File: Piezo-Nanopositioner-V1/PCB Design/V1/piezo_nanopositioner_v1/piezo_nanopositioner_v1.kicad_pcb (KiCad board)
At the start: 4 copper layers, 187.2 x 72.2 mm, 101 parts, among them J101 Conn_01x03_Pin, J201 Conn_01x10_Pin, J202 RF2-04A-T-00-50-G, J301 Conn_01x10_Pin, J302 RF2-04A-T-00-50-G, J401 Conn_01x10_Pin, J402 RF2-04A-T-00-50-G, U201 TL431AIDBZR, U202 DAC0800LCM, U203 TDA2050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

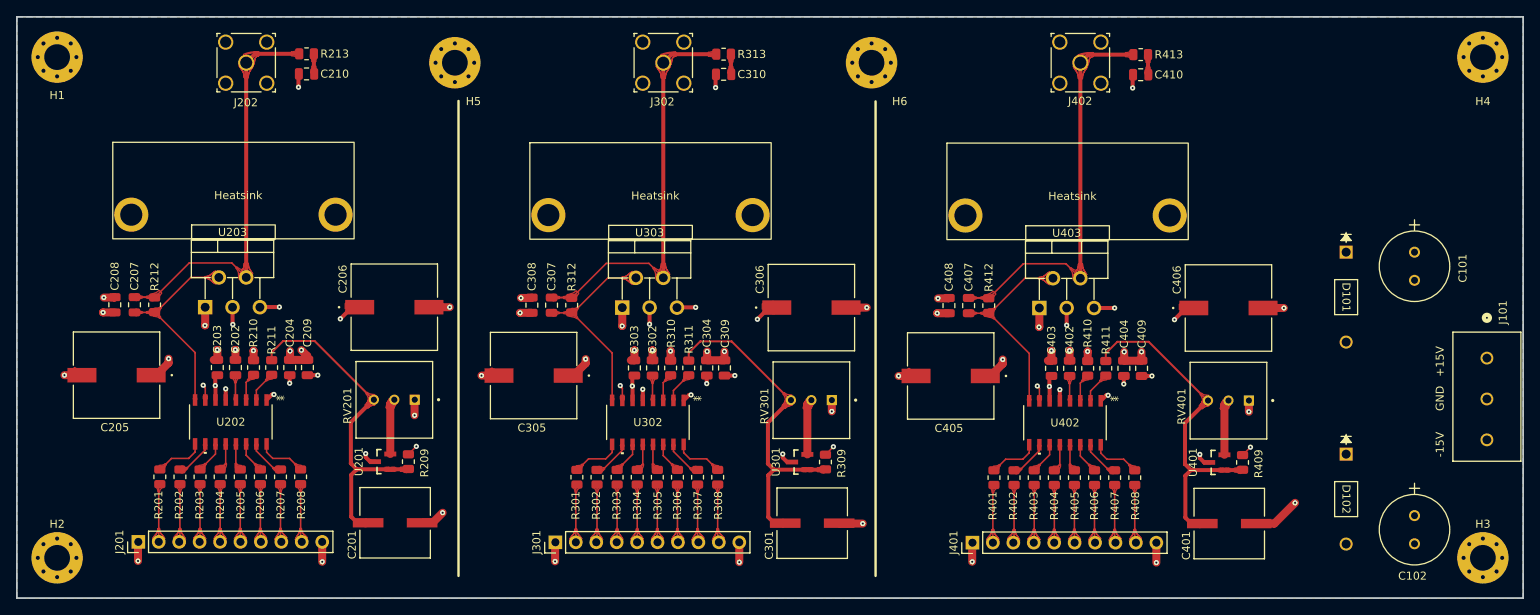
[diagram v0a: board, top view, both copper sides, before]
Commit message: added much needed polarity markings on silkscreen. Added testing rig files for testing your piezo element, clamps down the piezo and reads accelerometer data & temperatre (thermistor). Also added firmware for controlling piezo motion via Arduino Mega.
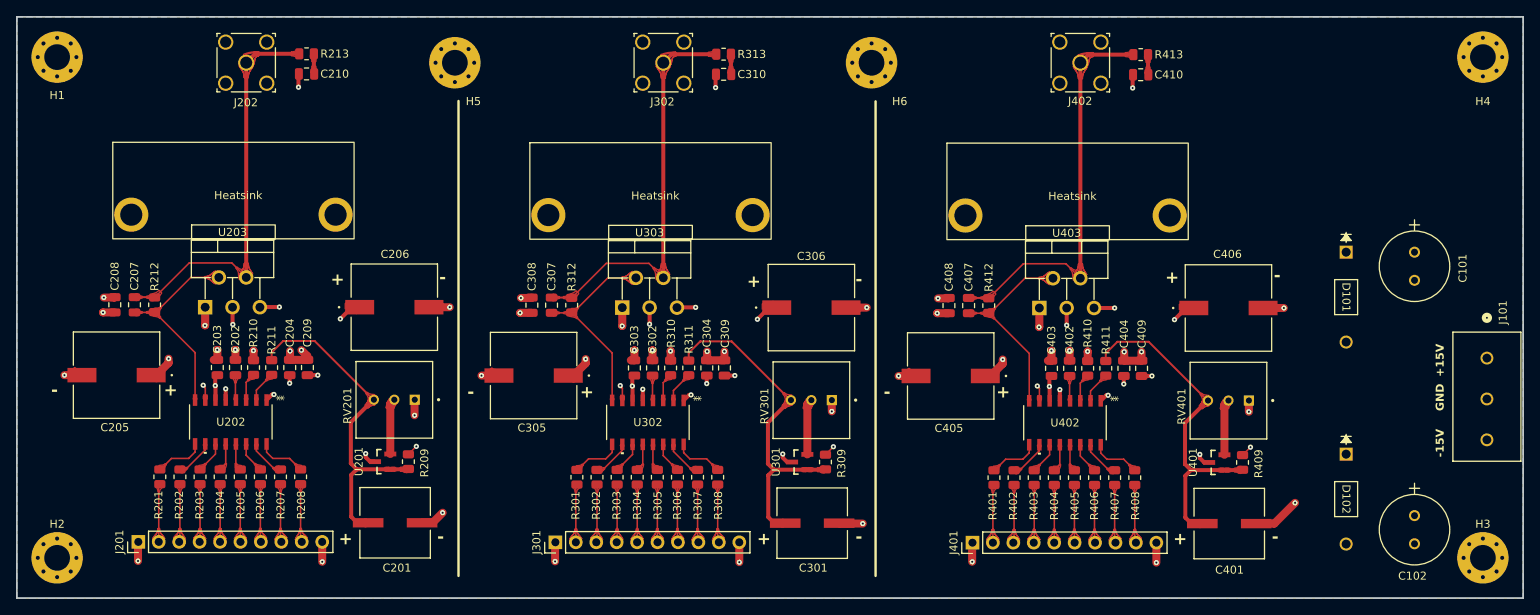
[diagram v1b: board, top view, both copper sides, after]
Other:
- board text added: "+"
- board text added: "-"
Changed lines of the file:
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@@
 		(tags "EEE-FC1E470P ")
 		(property "Reference" "C401"
-			(at -5.3528 2.75 90)
+			(at 0.03 5.76 0)
 			(unlocked yes)
 			(layer "F.SilkS")
@@
 		(tags "EEH-ZS1E471P ")
 		(property "Reference" "C306"
-			(at -6.4 -3.5 90)
+			(at -0.02 -6.39 0)
 			(unlocked yes)
 			(layer "F.SilkS")
@@
 		(tags "EEE-FC1E470P ")
 		(property "Reference" "C301"
-			(at -5.3528 2.75 90)
+			(at 0.13 5.56 0)
 			(unlocked yes)
 			(layer "F.SilkS")
@@
 		(tags "EEH-ZS1E471P ")
 		(property "Reference" "C206"
-			(at -6.4 -3.5 90)
+			(at 0.08 -6.59 0)
 			(unlocked yes)
 			(layer "F.SilkS")
@@
 		(tags "EEE-FC1E470P ")
 		(property "Reference" "C201"
-			(at -5.3528 2.75 90)
+			(at 0.23 5.61 0)
 			(unlocked yes)
 			(layer "F.SilkS")
@@
 		(tags "EEH-ZS1E471P ")
 		(property "Reference" "C406"
-			(at -6.4 -3.5 90)
+			(at -0.12 -6.69 0)
 			(unlocked yes)
 			(layer "F.SilkS")
@@
 		(layer "Edge.Cuts")
 	)
+	(gr_text "+"
+		(at 192 91 0)
+		(layer "F.SilkS")
+		(effects
+			(font
+				(size 1.5 1.5)
+				(thickness 0.375)
+				(bold yes)
+			)
+			(justify left bottom)
+		)
+	)
 	(gr_text "+15V"
 		(at 247.75 88.25 90)
@@
 			(font
 				(size 1 1)
-				(thickness 0.1)
+				(thickness 0.25)
+				(bold yes)
+			)
+			(justify left bottom)
+		)
+	)
+	(gr_text "-"
+		(at 226.5 76.5 0)
+		(layer "F.SilkS")
+		(effects
+			(font
+				(size 1.5 1.5)
+				(thickness 0.375)
+				(bold yes)
+			)
+			(justify left bottom)
+		)
+	)
+	(gr_text "-"
+		(at 174.5 77 0)
+		(layer "F.SilkS")
+		(effects
+			(font
+				(size 1.5 1.5)
+				(thickness 0.375)
+				(bold yes)
+			)
+			(justify left bottom)
+		)
+	)
+	(gr_text "-"
+		(at 74.5 90.75 0)
+		(layer "F.SilkS")
+		(effects
+			(font
+				(size 1.5 1.5)
+				(thickness 0.375)
+				(bold yes)
 			)
 			(justify left bottom)
@@
 			(font
 				(size 1 1)
-				(thickness 0.1)
+				(thickness 0.25)
+				(bold yes)
+			)
+			(justify left bottom)
+		)
+	)
+	(gr_text "+"
+		(at 140.25 91 0)
+		(layer "F.SilkS")
+		(effects
+			(font
+				(size 1.5 1.5)
+				(thickness 0.375)
+				(bold yes)
+			)
+			(justify left bottom)
+		)
+	)
+	(gr_text "+"
+		(at 214 109.25 0)
+		(layer "F.SilkS")
+		(effects
+			(font
+				(size 1.5 1.5)
+				(thickness 0.375)
+				(bold yes)
+			)
+			(justify left bottom)
+		)
+	)
+	(gr_text "-"
+		(at 122.5 109 0)
+		(layer "F.SilkS")
+		(effects
+			(font
+				(size 1.5 1.5)
+				(thickness 0.375)
+				(bold yes)
+			)
+			(justify left bottom)
+		)
+	)
+	(gr_text "+"
+		(at 161 77.25 0)
+		(layer "F.SilkS")
+		(effects
+			(font
+				(size 1.5 1.5)
+				(thickness 0.375)
+				(bold yes)
+			)
+			(justify left bottom)
+		)
+	)
+	(gr_text "+"
+		(at 88.5 90.75 0)
+		(layer "F.SilkS")
+		(effects
+			(font
+				(size 1.5 1.5)
+				(thickness 0.375)
+				(bold yes)
+			)
+			(justify left bottom)
+		)
+	)
+	(gr_text "+"
+		(at 109.25 77 0)
+		(layer "F.SilkS")
+		(effects
+			(font
+				(size 1.5 1.5)
+				(thickness 0.375)
+				(bold yes)
+			)
+			(justify left bottom)
+		)
+	)
+	(gr_text "-"
+		(at 178 91 0)
+		(layer "F.SilkS")
+		(effects
+			(font
+				(size 1.5 1.5)
+				(thickness 0.375)
+				(bold yes)
+			)
+			(justify left bottom)
+		)
+	)
+	(gr_text "+"
+		(at 162.25 109.25 0)
+		(layer "F.SilkS")
+		(effects
+			(font
+				(size 1.5 1.5)
+				(thickness 0.375)
+				(bold yes)
+			)
+			(justify left bottom)
+		)
+	)
+	(gr_text "+"
+		(at 110.25 109.25 0)
+		(layer "F.SilkS")
+		(effects
+			(font
+				(size 1.5 1.5)
+				(thickness 0.375)
+				(bold yes)
+			)
+			(justify left bottom)
+		)
+	)
+	(gr_text "+"
+		(at 213 76.75 0)
+		(layer "F.SilkS")
+		(effects
+			(font
+				(size 1.5 1.5)
+				(thickness 0.375)
+				(bold yes)
+			)
+			(justify left bottom)
+		)
+	)
+	(gr_text "-"
+		(at 174.5 109 0)
+		(layer "F.SilkS")
+		(effects
+			(font
+				(size 1.5 1.5)
+				(thickness 0.375)
+				(bold yes)
+			)
+			(justify left bottom)
+		)
+	)
+	(gr_text "-"
+		(at 126.25 91 0)
+		(layer "F.SilkS")
+		(effects
+			(font
+				(size 1.5 1.5)
+				(thickness 0.375)
+				(bold yes)
+			)
+			(justify left bottom)
+		)
+	)
+	(gr_text "-"
+		(at 122.75 76.75 0)
+		(layer "F.SilkS")
+		(effects
+			(font
+				(size 1.5 1.5)
+				(thickness 0.375)
+				(bold yes)
 			)
 			(justify left bottom)
@@
 			(font
 				(size 1 1)
-				(thickness 0.1)
+				(thickness 0.25)
+				(bold yes)
+			)
+			(justify left bottom)
+		)
+	)
+	(gr_text "-"
+		(at 226.25 109 0)
+		(layer "F.SilkS")
+		(effects
+			(font
+				(size 1.5 1.5)
+				(thickness 0.375)
+				(bold yes)
 			)
 			(justify left bottom)
